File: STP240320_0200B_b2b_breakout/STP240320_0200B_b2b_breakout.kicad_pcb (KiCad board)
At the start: 2 copper layers, 35.6 x 59.2 mm, 18 parts, among them J1 Micro_SD_Card_Det_Hirose_DM3AT, J2 Conn_01x11, Q1 BSS138, U1 74HC4050D, U2 AP2112K-3.3, U3 LM809M3X-2.93

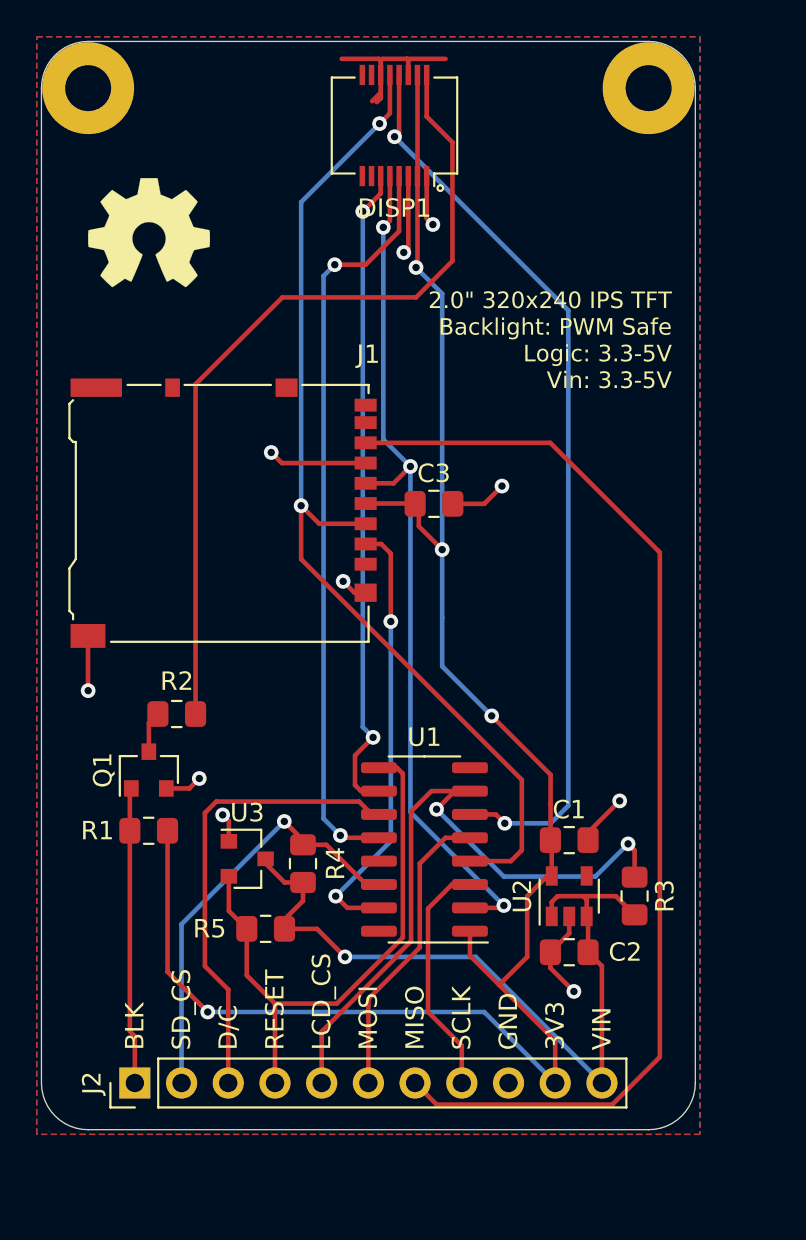
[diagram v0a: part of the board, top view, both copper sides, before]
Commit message: kicad: update to kicad 6
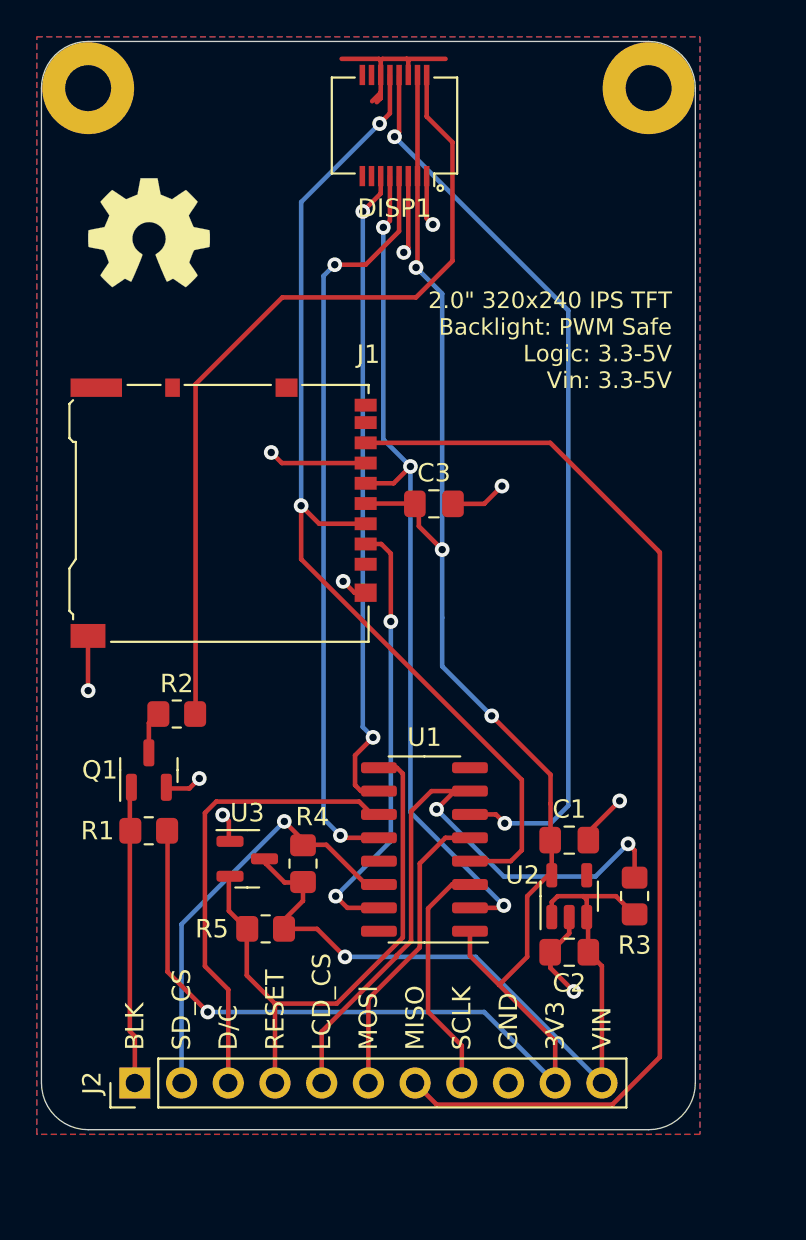
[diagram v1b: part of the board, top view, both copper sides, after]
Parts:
- C1, C2, C3: footprint Capacitor_SMD:C_0805_2012Metric_Pad1.15x1.40mm_HandSolder -> Capacitor_SMD:C_0805_2012Metric_Pad1.18x1.45mm_HandSolder
- R1, R2, R3, R4, R5: footprint Resistor_SMD:R_0805_2012Metric_Pad1.15x1.40mm_HandSolder -> Resistor_SMD:R_0805_2012Metric_Pad1.20x1.40mm_HandSolder
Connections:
- J1 pad 1: Net-(J1-Pad1) -> unconnected-(J1-Pad1)
- J1 pad 10: Net-(J1-Pad10) -> unconnected-(J1-Pad10)
- J1 pad 8: Net-(J1-Pad8) -> unconnected-(J1-Pad8)
- J1 pad 9: Net-(J1-Pad9) -> unconnected-(J1-Pad9)
- U2 pad 4: Net-(U2-Pad4) -> unconnected-(U2-Pad4)
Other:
- net class Default removed

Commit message: ci: add release support
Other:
- board text added: "${TAG} (${REVISION})"
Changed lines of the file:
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@@
     )
   )
+  (property "DATE" "YYYY-MM-DD HH:MM:SS")
+  (property "REVISION" "REVISION")
+  (property "TAG" "TAG")
   (net 0 "")
   (net 1 "Net-(DISP1-Pad2)")
@@
     (effects (font (size 1 1) (thickness 0.15)) (justify left))
   )
+  (gr_text "${TAG}\n(${REVISION})" (at 28.321 29.845) (layer "F.SilkS")
+    (effects (font (size 1 1) (thickness 0.15)))
+  )
   (segment (start 20.95 4.0844) (end 20.95 1.822) (width 0.25) (layer "F.Cu") (net 1))

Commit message: Revert "ci: add release support (#2)"
This reverts commit f3a1c30362bc760beaf5669eca90d55fbc6df8b2.
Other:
- board text removed: "${TAG} (${REVISION})"
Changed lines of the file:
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@@
     )
   )
-  (property "DATE" "YYYY-MM-DD HH:MM:SS")
-  (property "REVISION" "REVISION")
-  (property "TAG" "TAG")
   (net 0 "")
   (net 1 "Net-(DISP1-Pad2)")
@@
     (effects (font (size 1 1) (thickness 0.15)) (justify left))
   )
-  (gr_text "${TAG}\n(${REVISION})" (at 28.321 29.845) (layer "F.SilkS")
-    (effects (font (size 1 1) (thickness 0.15)))
-  )
   (segment (start 20.95 4.0844) (end 20.95 1.822) (width 0.25) (layer "F.Cu") (net 1))
